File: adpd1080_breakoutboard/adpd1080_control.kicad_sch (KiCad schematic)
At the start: 16 parts, among them IC1 ADPD1080BCPZR7, J4 P_05, J5 P_01, J6 PD_7, J7 P_3_LED, J8 P_1, U2 TXB0104PW_new

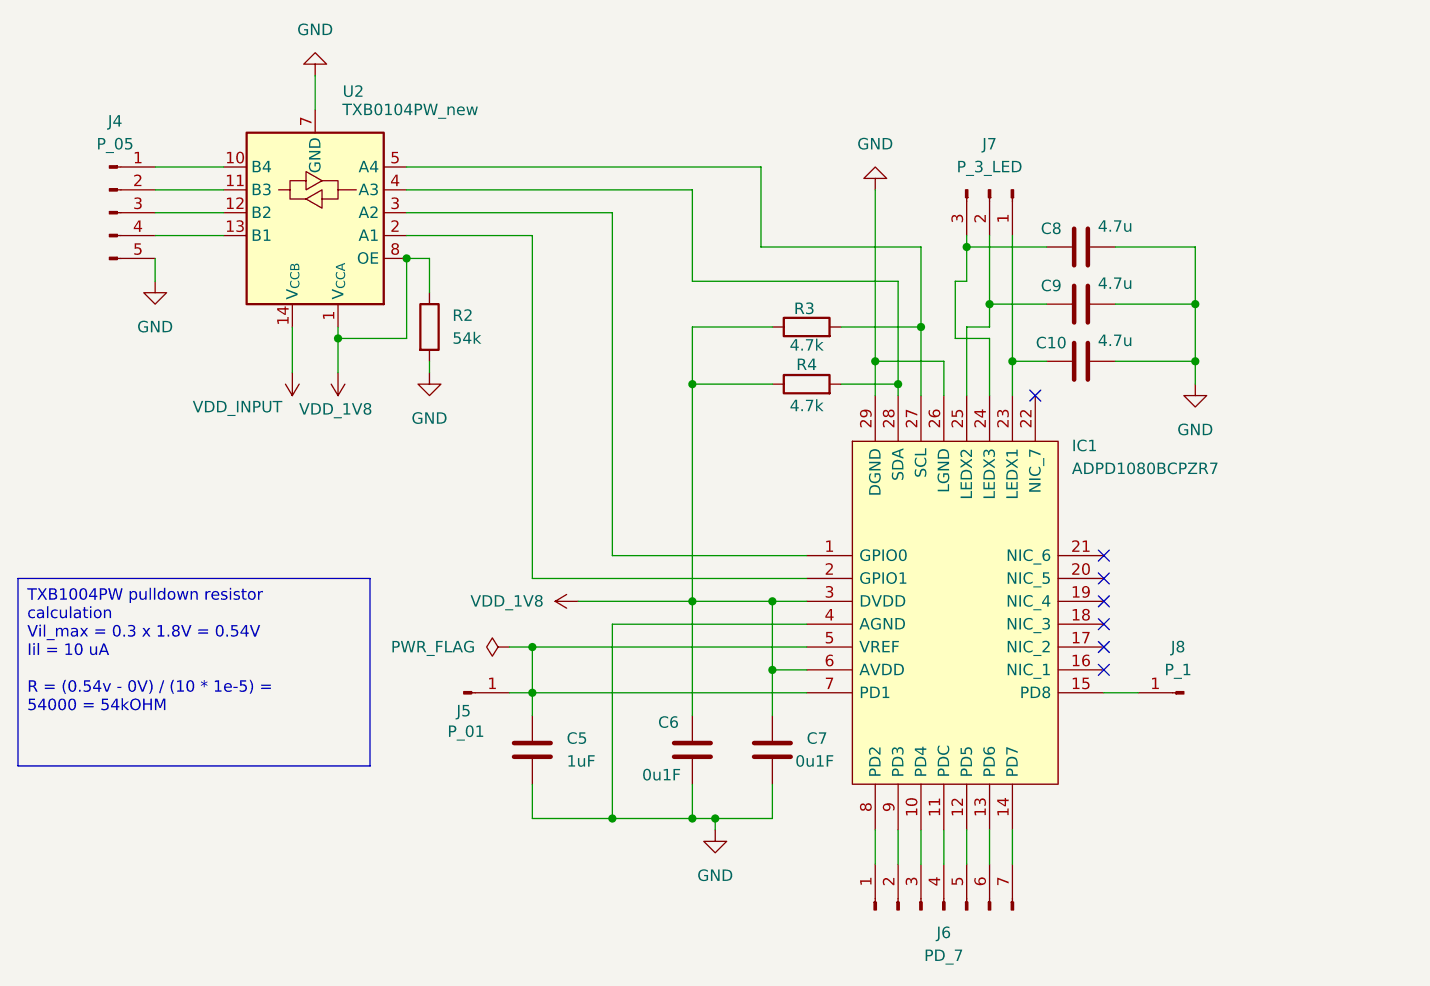
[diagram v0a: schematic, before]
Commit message: removed caps that were in wrong side of ledx
Signed-off-by: Mika Laitio <lamikr@gmail.com>
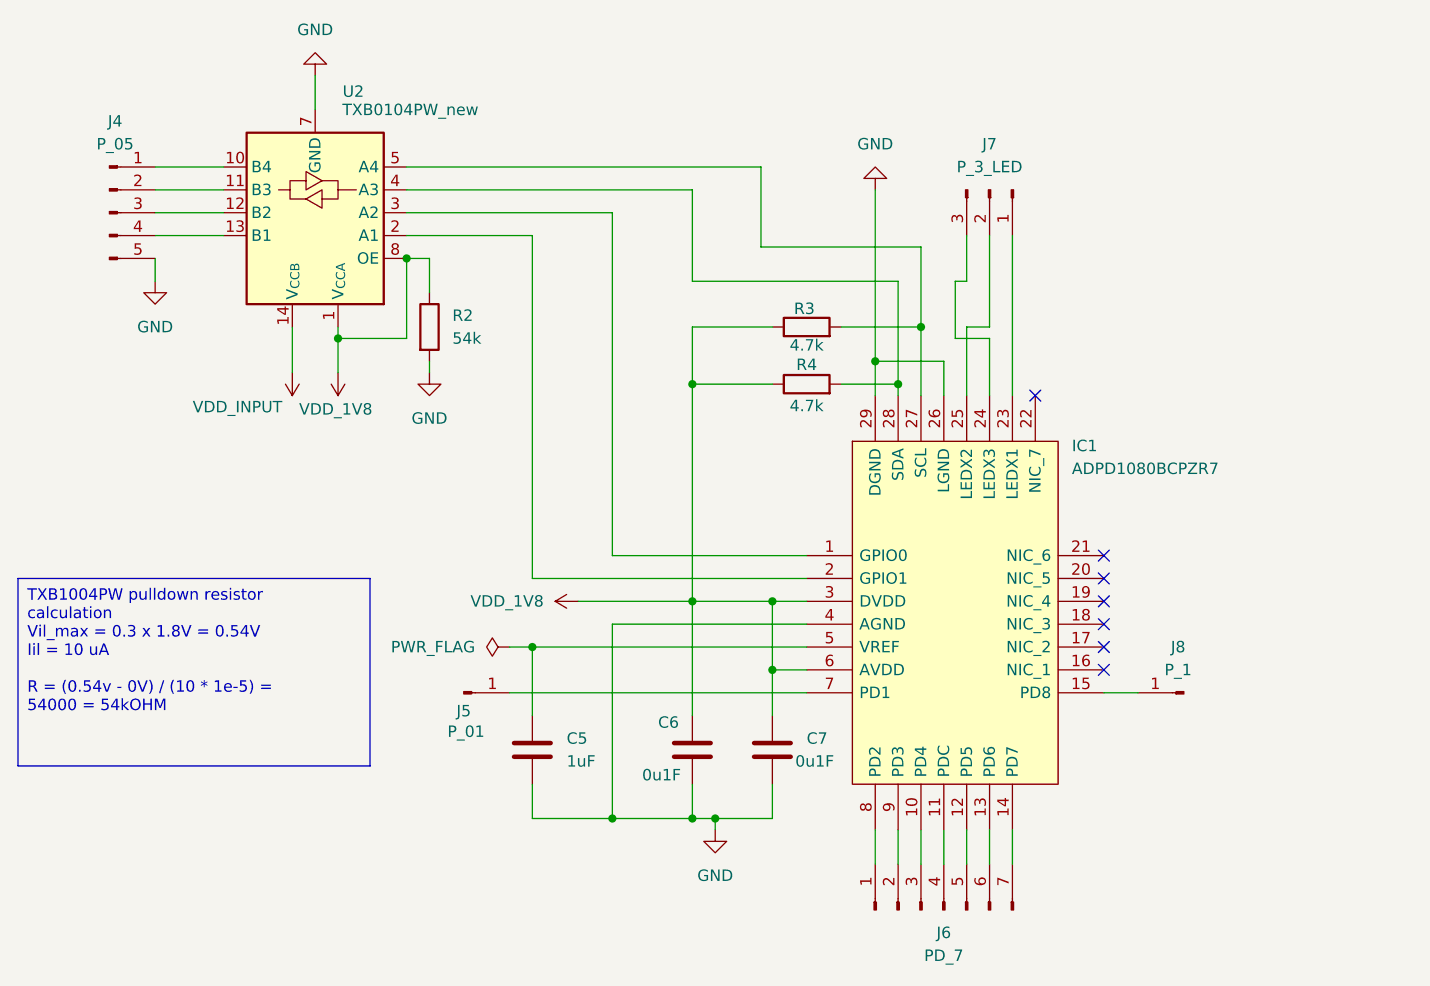
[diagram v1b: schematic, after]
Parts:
- removed C10, C8, C9: 4.7u, Capacitor_SMD:C_0402_1005Metric, symbol Device:C
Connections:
- net at C5.1, IC1.5 (VREF): no longer IC1.7 (PD1), J5.1 (Pin_1)
- new net: IC1.7 (PD1), J5.1 (Pin_1)

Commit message: replace txb0104 with txs0104e for i2c
- txb0104 does not work with i2c but txs0104e works
- changed the i2c pull-ups to 'no-placement' because
  the txs0104e has internal 10k pull-ups
- added test points for 1v8 logic scl and sda

Signed-off-by: Mika Laitio <lamikr@gmail.com>
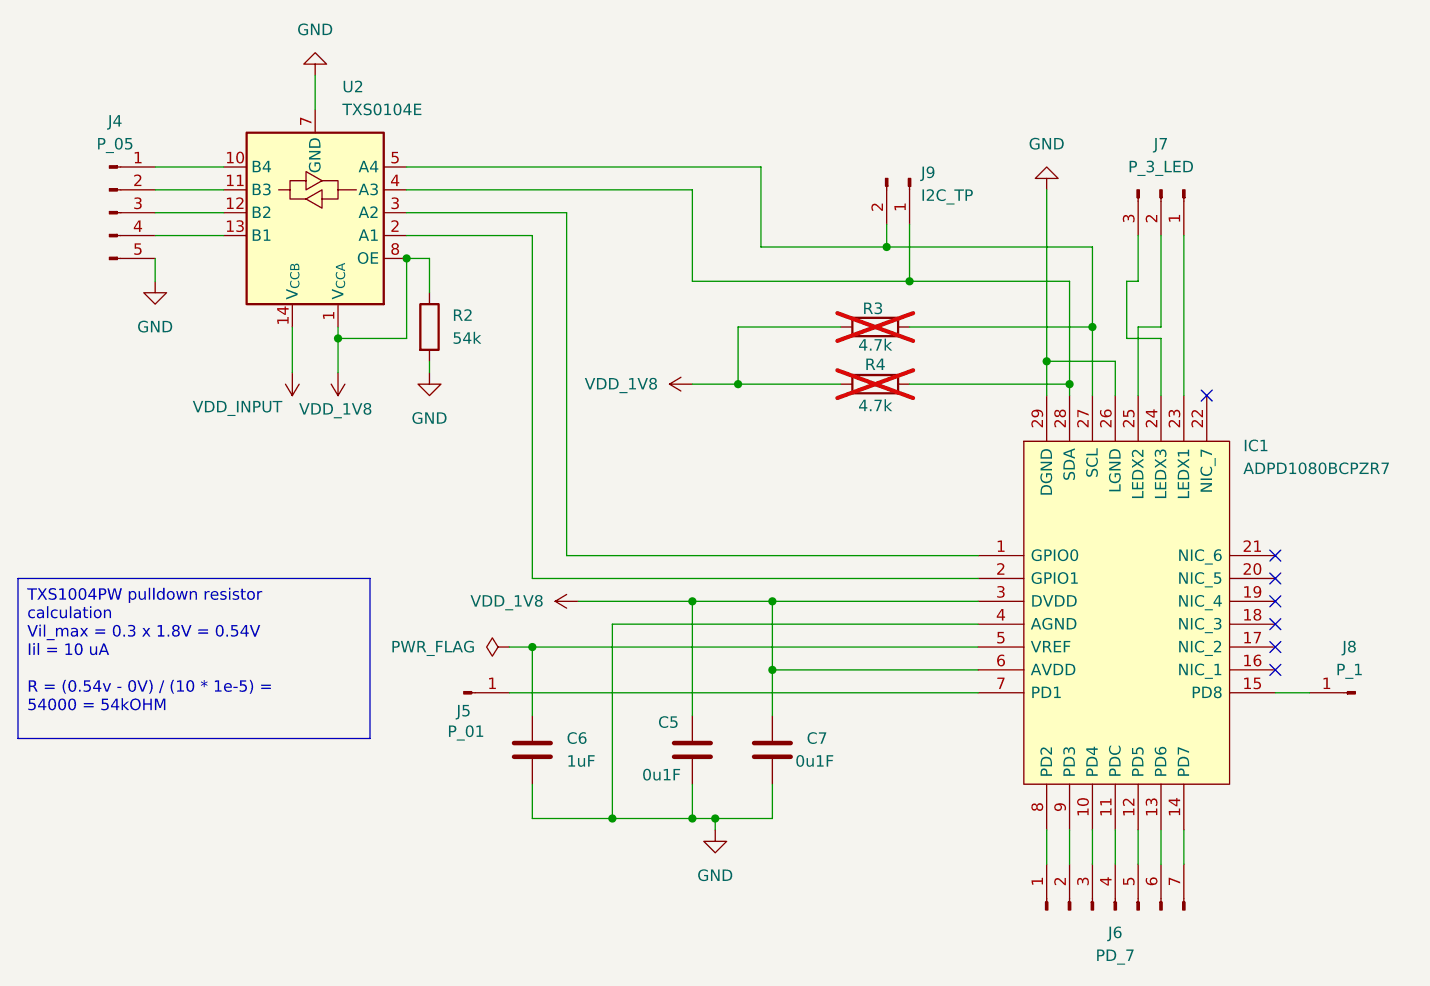
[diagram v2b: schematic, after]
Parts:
- removed U2: TXB0104PW_new, Package_SO:TSSOP-14_4.4x5mm_P0.65mm, symbol breakoutboard:TXB0104PW_new
- added J9: I2C_TP, Connector_PinHeader_1.27mm:PinHeader_1x02_P1.27mm_Vertical, symbol Connector:Conn_01x02_Pin
- added U2: TXS0104E, Package_SO:TSSOP-14_4.4x5mm_P0.65mm, symbol breakoutboard:TXS0104E
- R3, R4: now not fitted
- renumbered C6 to C5, C5 to C6
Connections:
- net GND: now also U2.7 (GND)
- net VDD_1V8: now also U2.1 (V_{CCA}), U2.8 (OE)
- net VDD_INPUT: now also U2.14 (V_{CCB})
- net at J4.1 (Pin_1): now also U2.10 (B4)
- net at J4.2 (Pin_2): now also U2.11 (B3)
- net at J4.3 (Pin_3): now also U2.12 (B2)
- net at J4.4 (Pin_4): now also U2.13 (B1)
- net at IC1.2 (GPIO1): now also U2.2 (A1)
- net at IC1.1 (GPIO0): now also U2.3 (A2)
- net at IC1.28 (SDA), R4.2: now also J9.1 (Pin_1), U2.4 (A3)
- net at IC1.27 (SCL), R3.2: now also J9.2 (Pin_2), U2.5 (A4)
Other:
- title: (none) -> ADPD1080 Breakoutboard
- moved on the sheet: IC1, J6, J7, J8
